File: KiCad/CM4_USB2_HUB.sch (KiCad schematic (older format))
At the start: 33 parts, among them IC1 USB2517-JZX, J10 72309-8014BLF, J11 10104110-0001LF, J12 SS-52100-002, J8 Conn_02x05_Odd_Even, J9 Conn_02x05_Odd_Even, U3 FSUSB42MUX, Y1 24MHz

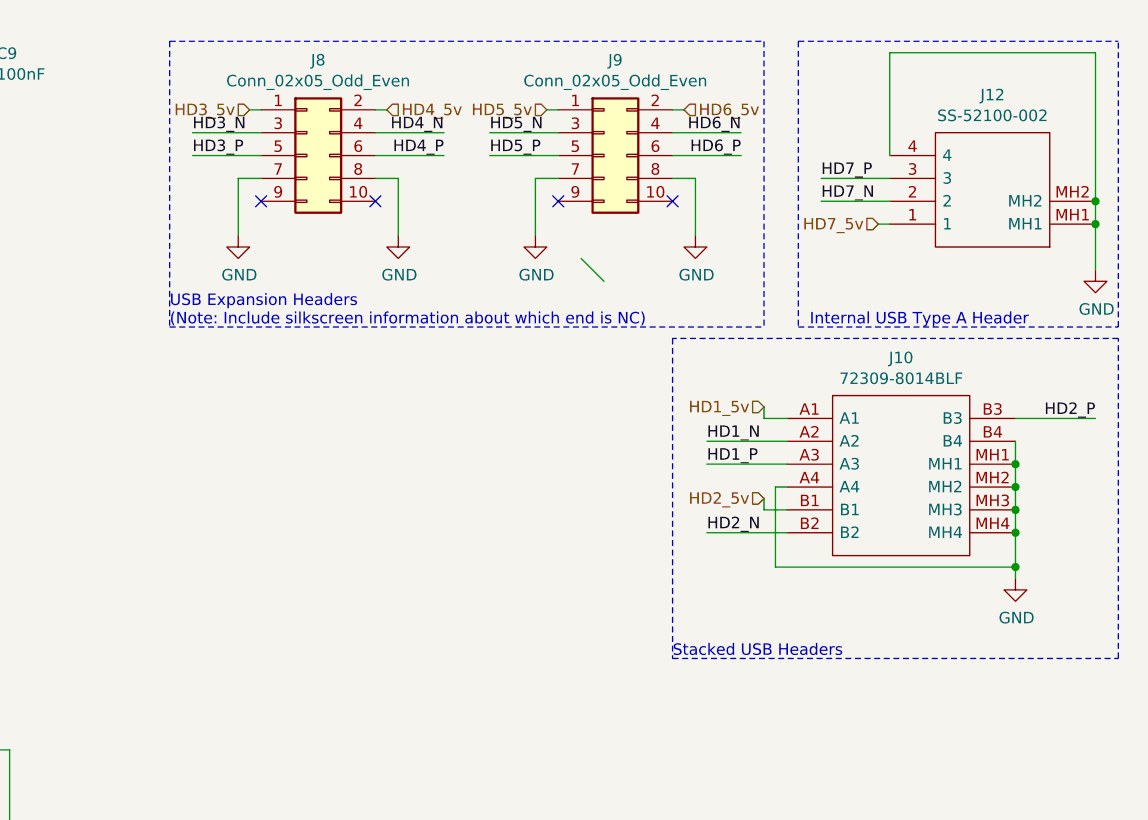
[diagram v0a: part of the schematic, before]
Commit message: Added second USB dual-stack header and fixed some library references.
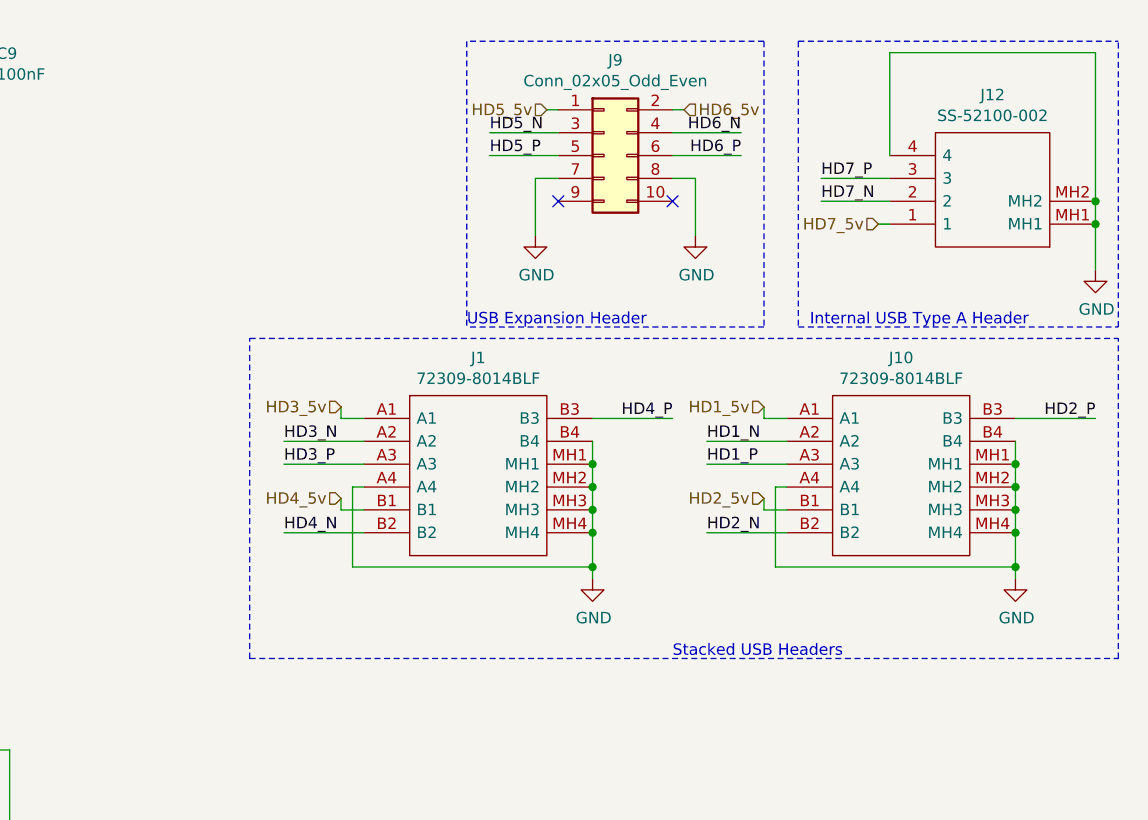
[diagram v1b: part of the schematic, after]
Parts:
- removed J8: Conn_02x05_Odd_Even, CM4_MATX:PinHeader_2x05_P2.54mm_Vertical, symbol Connector_Generic:Conn_02x05_Odd_Even
- added J1: 72309-8014BLF, CM4_MATX:723098014BLF, symbol CM4_MATX:72309-8014BLF
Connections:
- net GND: now also J1.A4, J1.B4, J1.MH1, J1.MH2, J1.MH3, J1.MH4
- net HD3_5v: now also J1.A1
- net HD3_N: now also J1.A2
- net HD3_P: now also J1.A3
- net HD4_5v: now also J1.B1
- net HD4_N: now also J1.B2
- net HD4_P: now also J1.B3
- no-connect marks 19 -> 17
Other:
- note added: "USB Expansion Header"
- note removed: "USB Expansion Headers\n(Note: Include silkscreen information about which end is NC)"
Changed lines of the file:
@@
 	9350 2750 9700 2750
 Wire Notes Line
-	9200 3300 11150 3300
-Wire Notes Line
 	11150 3300 11150 1900
-Wire Notes Line
-	11150 1900 9200 1900
-Wire Notes Line
-	9200 1900 9200 3300
 Text Notes 9200 3300 0    50   ~ 0
 Stacked USB Headers
@@
 	1    0    0    -1
 $EndComp
-$Comp
-L power:GND #PWR0126
-U 1 1 5FF0B6D3
-P 8000 1450
-F 0 "#PWR0126" H 8000 1200 50  0001 C CNN
-F 1 "GND" H 8005 1277 50  0000 C CNN
-F 2 "" H 8000 1450 50  0001 C CNN
-F 3 "" H 8000 1450 50  0001 C CNN
-	1    8000 1450
-	1    0    0    -1
-$EndComp
-$Comp
-L power:GND #PWR0127
-U 1 1 5FF0AFE9
-P 7300 1450
-F 0 "#PWR0127" H 7300 1200 50  0001 C CNN
-F 1 "GND" H 7305 1277 50  0000 C CNN
-F 2 "" H 7300 1450 50  0001 C CNN
-F 3 "" H 7300 1450 50  0001 C CNN
-	1    7300 1450
-	1    0    0    -1
-$EndComp
-NoConn ~ 7400 1300
-NoConn ~ 7900 1300
-Wire Wire Line
-	8000 1200 8000 1450
-Wire Wire Line
-	7900 1200 8000 1200
-Wire Wire Line
-	7300 1200 7300 1450
-Wire Wire Line
-	7400 1200 7300 1200
-Wire Wire Line
-	7400 1100 7100 1100
-Wire Wire Line
-	7100 1000 7400 1000
-Wire Wire Line
-	7900 1000 8200 1000
-Wire Wire Line
-	8200 1100 7900 1100
 Wire Wire Line
 	8700 1100 8400 1100
@@
 Text Label 8400 1000 0    50   ~ 0
 HD5_N
-Text Label 8200 1100 2    50   ~ 0
-HD4_P
-Text Label 8200 1000 2    50   ~ 0
-HD4_N
-Text Label 7100 1100 0    50   ~ 0
-HD3_P
-Text Label 7100 1000 0    50   ~ 0
-HD3_N
-$Comp
-L Connector_Generic:Conn_02x05_Odd_Even J8
-U 1 1 5FEAE38F
-P 7600 1100
-F 0 "J8" H 7650 1517 50  0000 C CNN
-F 1 "Conn_02x05_Odd_Even" H 7650 1426 50  0000 C CNN
-F 2 "CM4_MATX:PinHeader_2x05_P2.54mm_Vertical" H 7600 1100 50  0001 C CNN
-F 3 "~" H 7600 1100 50  0001 C CNN
-	1    7600 1100
-	1    0    0    -1
-$EndComp
 Wire Notes Line
 	9600 600  9600 1850
-Text Notes 7000 1850 0    50   ~ 0
-USB Expansion Headers\n(Note: Include silkscreen information about which end is NC)
+Text Notes 8300 1850 0    50   ~ 0
+USB Expansion Header
 Wire Wire Line
 	4850 3900 5200 3900
@@
 Wire Notes Line
 	9750 1850 11150 1850
-Text HLabel 7350 900  0    50   Input ~ 0
-HD3_5v
-Wire Wire Line
-	7350 900  7400 900
-Text HLabel 7950 900  2    50   Input ~ 0
-HD4_5v
 Text HLabel 8650 900  0    50   Input ~ 0
 HD5_5v
 Wire Wire Line
 	8650 900  8700 900
-Wire Wire Line
-	7900 900  7950 900
 Text HLabel 9250 900  2    50   Input ~ 0
 HD6_5v
 Wire Wire Line
 	9250 900  9200 900
-Wire Notes Line
-	7000 600  7000 1850
-Wire Notes Line
-	7000 600  9600 600
-Wire Notes Line
-	7000 1850 9600 1850
 Text HLabel 9600 2600 0    50   Input ~ 0
 HD2_5v
@@
 Text Notes 7550 6500 0    50   ~ 0
 USB OTG/Slave connector for eMMC flashing on support CM4s
-Entry Wire Line
-	8800 1550 8900 1650
+$Comp
+L CM4_MATX:72309-8014BLF J1
+U 1 1 626F6425
+P 7850 2250
+F 0 "J1" H 8350 2515 50  0000 C CNN
+F 1 "72309-8014BLF" H 8350 2424 50  0000 C CNN
+F 2 "CM4_MATX:723098014BLF" H 8700 2350 50  0001 L CNN
+F 3 "https://cdn.amphenol-icc.com/media/wysiwyg/files/drawing/72309.pdf" H 8700 2250 50  0001 L CNN
+F 4 "USB Connectors 8P R/A RECPT" H 8700 2150 50  0001 L CNN "Description"
+F 5 "15" H 8700 2050 50  0001 L CNN "Height"
+F 6 "649-72309-8014BLF" H 8700 1950 50  0001 L CNN "Mouser Part Number"
+F 7 "https://www.mouser.co.uk/ProductDetail/Amphenol-FCI/72309-8014BLF?qs=D%252By4jQJzx8Iuk4xBbyHrOA%3D%3D" H 8700 1850 50  0001 L CNN "Mouser Price/Stock"
+F 8 "Amphenol" H 8700 1750 50  0001 L CNN "Manufacturer_Name"
+F 9 "72309-8014BLF" H 8700 1650 50  0001 L CNN "Manufacturer_Part_Number"
+	1    7850 2250
+	1    0    0    -1
+$EndComp
+Wire Wire Line
+	8850 2450 8850 2550
+Connection ~ 8850 2550
+Wire Wire Line
+	8850 2550 8850 2650
+Connection ~ 8850 2650
+Wire Wire Line
+	8850 2650 8850 2750
+Connection ~ 8850 2750
+Wire Wire Line
+	8850 2750 8850 2900
+$Comp
+L power:GND #PWR0103
+U 1 1 626F6432
+P 8850 2950
+F 0 "#PWR0103" H 8850 2700 50  0001 C CNN
+F 1 "GND" H 8855 2777 50  0000 C CNN
+F 2 "" H 8850 2950 50  0001 C CNN
+F 3 "" H 8850 2950 50  0001 C CNN
+	1    8850 2950
+	1    0    0    -1
+$EndComp
+Text Label 7500 2350 0    50   ~ 0
+HD3_N
+Text Label 7500 2450 0    50   ~ 0
+HD3_P
+Text Label 7500 2750 0    50   ~ 0
+HD4_N
+Text Label 9200 2250 2    50   ~ 0
+HD4_P
+Wire Wire Line
+	9200 2250 8850 2250
+Wire Wire Line
+	7500 2350 7850 2350
+Wire Wire Line
+	7850 2450 7500 2450
+Wire Wire Line
+	7850 2550 7800 2550
+Wire Wire Line
+	7800 2550 7800 2900
+Wire Wire Line
+	7800 2900 8850 2900
+Connection ~ 8850 2900
+Wire Wire Line
+	8850 2900 8850 2950
+Wire Wire Line
+	8850 2350 8850 2450
+Connection ~ 8850 2450
+Wire Wire Line
+	7500 2750 7850 2750
+Text HLabel 7750 2200 0    50   Input ~ 0
+HD3_5v
+Text HLabel 7750 2600 0    50   Input ~ 0
+HD4_5v
+Wire Wire Line
+	7750 2600 7750 2650
+Wire Wire Line
+	7750 2650 7850 2650
+Wire Wire Line
+	7750 2200 7750 2250
+Wire Wire Line
+	7750 2250 7850 2250
+Wire Notes Line
+	7350 3300 7350 1900
+Wire Notes Line
+	7350 3300 11150 3300
+Wire Notes Line
+	7350 1900 11150 1900
+Wire Notes Line
+	8300 600  8300 1850
+Wire Notes Line
+	9600 600  8300 600
+Wire Notes Line
+	9600 1850 8300 1850
 $EndSCHEMATC

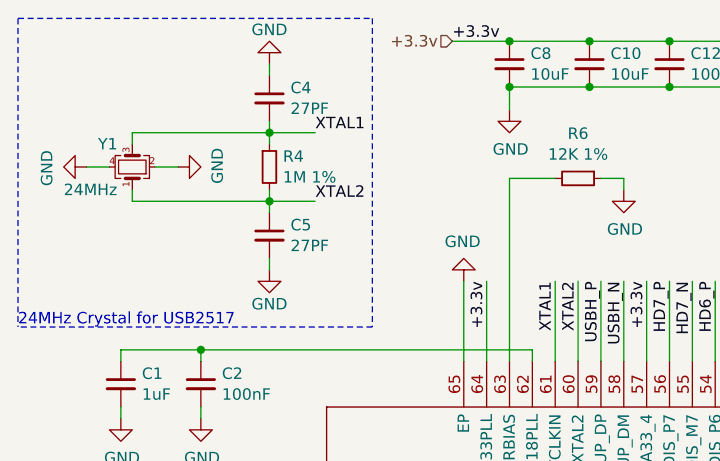
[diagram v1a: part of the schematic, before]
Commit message: PCIe Wiring, resistor value adjustments, and a bunch of small ERC fixes.
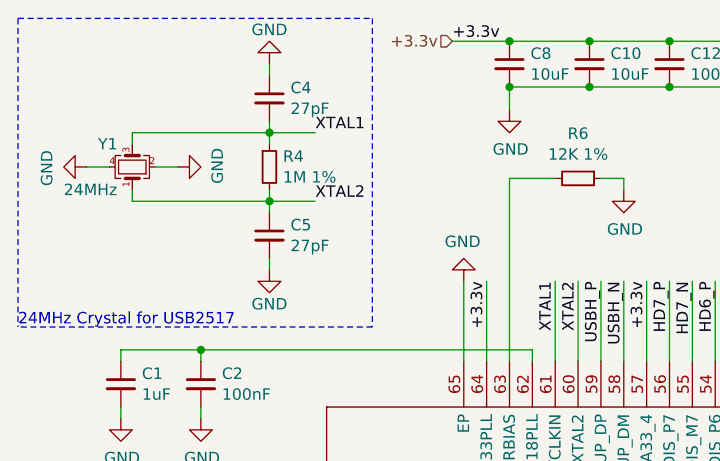
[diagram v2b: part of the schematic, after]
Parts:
- C4, C5: value 27PF -> 27pF
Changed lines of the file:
@@
 P 1600 1450
 F 0 "C5" H 1692 1496 50  0000 L CNN
-F 1 "27PF" H 1692 1405 50  0000 L CNN
+F 1 "27pF" H 1692 1405 50  0000 L CNN
 F 2 "" H 1600 1450 50  0001 C CNN
 F 3 "~" H 1600 1450 50  0001 C CNN
@@
 P 1600 850
 F 0 "C4" H 1692 896 50  0000 L CNN
-F 1 "27PF" H 1692 805 50  0000 L CNN
+F 1 "27pF" H 1692 805 50  0000 L CNN
 F 2 "" H 1600 850 50  0001 C CNN
 F 3 "~" H 1600 850 50  0001 C CNN

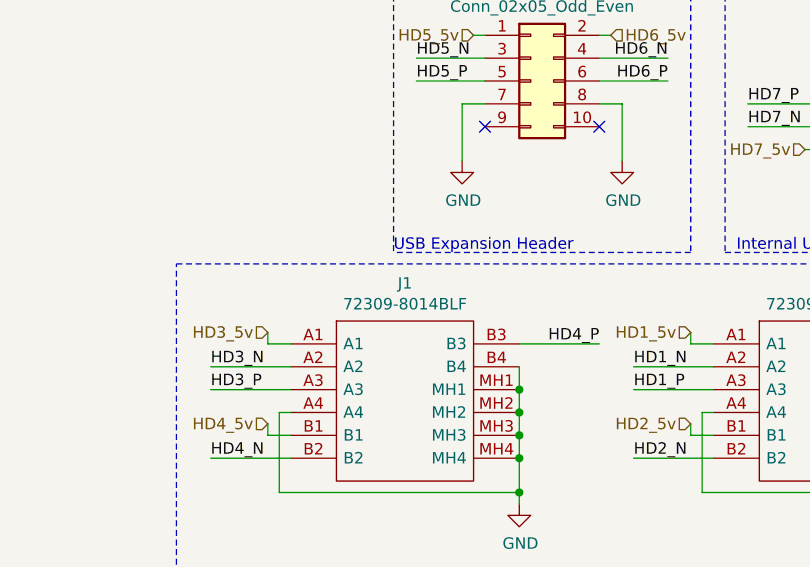
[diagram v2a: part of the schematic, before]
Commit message: Updated CM4 footprints/symbols, mounting holes
This is in a bid to make it more manufactuerable by reducing the need for explanations and questions.
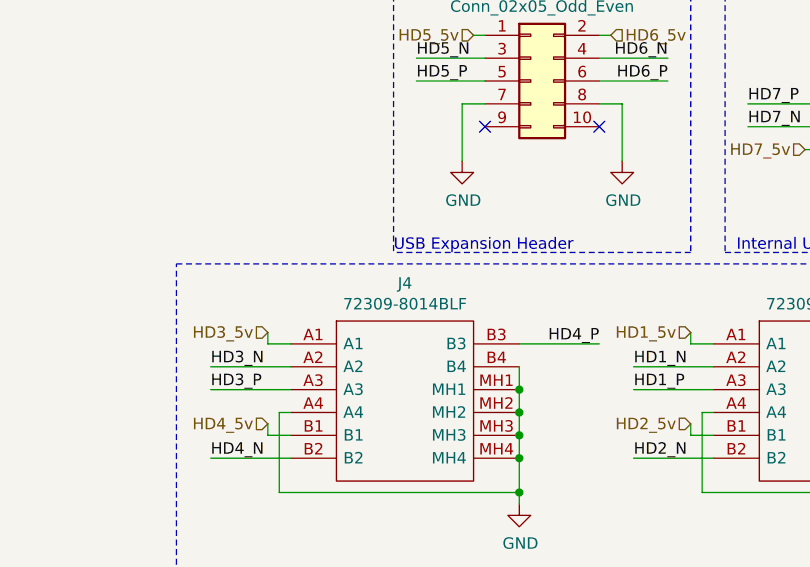
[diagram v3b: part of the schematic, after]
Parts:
- renumbered J1 to J4
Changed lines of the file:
@@
 Sheet 8 16
 Title "CM4_MATX: USB Hub and Ports"
-Date "2020-12-28"
+Date "2021-02-08"
 Rev "0.1"
 Comp "Copyright Oliver Møller/@TheGuyDanish 2020, CERN OHL-P v2"
@@
 Text Notes 7550 6500 0    50   ~ 0
 USB OTG/Slave connector for eMMC flashing on support CM4s
-$Comp
-L CM4_MATX:72309-8014BLF J1
+Wire Wire Line
+	8850 2450 8850 2550
+Connection ~ 8850 2550
+Wire Wire Line
+	8850 2550 8850 2650
+Connection ~ 8850 2650
+Wire Wire Line
+	8850 2650 8850 2750
+Connection ~ 8850 2750
+Wire Wire Line
+	8850 2750 8850 2900
+$Comp
+L power:GND #PWR0103
+U 1 1 626F6432
+P 8850 2950
+F 0 "#PWR0103" H 8850 2700 50  0001 C CNN
+F 1 "GND" H 8855 2777 50  0000 C CNN
+F 2 "" H 8850 2950 50  0001 C CNN
+F 3 "" H 8850 2950 50  0001 C CNN
+	1    8850 2950
+	1    0    0    -1
+$EndComp
+Text Label 7500 2350 0    50   ~ 0
+HD3_N
+Text Label 7500 2450 0    50   ~ 0
+HD3_P
+Text Label 7500 2750 0    50   ~ 0
+HD4_N
+Text Label 9200 2250 2    50   ~ 0
+HD4_P
+Wire Wire Line
+	9200 2250 8850 2250
+Wire Wire Line
+	7500 2350 7850 2350
+Wire Wire Line
+	7850 2450 7500 2450
+Wire Wire Line
+	7850 2550 7800 2550
+Wire Wire Line
+	7800 2550 7800 2900
+Wire Wire Line
+	7800 2900 8850 2900
+Connection ~ 8850 2900
+Wire Wire Line
+	8850 2900 8850 2950
+Wire Wire Line
+	8850 2350 8850 2450
+Connection ~ 8850 2450
+Wire Wire Line
+	7500 2750 7850 2750
+Text HLabel 7750 2200 0    50   Input ~ 0
+HD3_5v
+Text HLabel 7750 2600 0    50   Input ~ 0
+HD4_5v
+Wire Wire Line
+	7750 2600 7750 2650
+Wire Wire Line
+	7750 2650 7850 2650
+Wire Wire Line
+	7750 2200 7750 2250
+Wire Wire Line
+	7750 2250 7850 2250
+Wire Notes Line
+	7350 3300 7350 1900
+Wire Notes Line
+	7350 3300 11150 3300
+Wire Notes Line
+	7350 1900 11150 1900
+Wire Notes Line
+	8300 600  8300 1850
+Wire Notes Line
+	9600 600  8300 600
+Wire Notes Line
+	9600 1850 8300 1850
+$Comp
+L CM4_MATX:72309-8014BLF J4
 U 1 1 626F6425
 P 7850 2250
-F 0 "J1" H 8350 2515 50  0000 C CNN
+F 0 "J4" H 8350 2515 50  0000 C CNN
 F 1 "72309-8014BLF" H 8350 2424 50  0000 C CNN
 F 2 "CM4_MATX:723098014BLF" H 8700 2350 50  0001 L CNN
@@
 	1    0    0    -1
 $EndComp
-Wire Wire Line
-	8850 2450 8850 2550
-Connection ~ 8850 2550
-Wire Wire Line
-	8850 2550 8850 2650
-Connection ~ 8850 2650
-Wire Wire Line
-	8850 2650 8850 2750
-Connection ~ 8850 2750
-Wire Wire Line
-	8850 2750 8850 2900
-$Comp
-L power:GND #PWR0103
-U 1 1 626F6432
-P 8850 2950
-F 0 "#PWR0103" H 8850 2700 50  0001 C CNN
-F 1 "GND" H 8855 2777 50  0000 C CNN
-F 2 "" H 8850 2950 50  0001 C CNN
-F 3 "" H 8850 2950 50  0001 C CNN
-	1    8850 2950
-	1    0    0    -1
-$EndComp
-Text Label 7500 2350 0    50   ~ 0
-HD3_N
-Text Label 7500 2450 0    50   ~ 0
-HD3_P
-Text Label 7500 2750 0    50   ~ 0
-HD4_N
-Text Label 9200 2250 2    50   ~ 0
-HD4_P
-Wire Wire Line
-	9200 2250 8850 2250
-Wire Wire Line
-	7500 2350 7850 2350
-Wire Wire Line
-	7850 2450 7500 2450
-Wire Wire Line
-	7850 2550 7800 2550
-Wire Wire Line
-	7800 2550 7800 2900
-Wire Wire Line
-	7800 2900 8850 2900
-Connection ~ 8850 2900
-Wire Wire Line
-	8850 2900 8850 2950
-Wire Wire Line
-	8850 2350 8850 2450
-Connection ~ 8850 2450
-Wire Wire Line
-	7500 2750 7850 2750
-Text HLabel 7750 2200 0    50   Input ~ 0
-HD3_5v
-Text HLabel 7750 2600 0    50   Input ~ 0
-HD4_5v
-Wire Wire Line
-	7750 2600 7750 2650
-Wire Wire Line
-	7750 2650 7850 2650
-Wire Wire Line
-	7750 2200 7750 2250
-Wire Wire Line
-	7750 2250 7850 2250
-Wire Notes Line
-	7350 3300 7350 1900
-Wire Notes Line
-	7350 3300 11150 3300
-Wire Notes Line
-	7350 1900 11150 1900
-Wire Notes Line
-	8300 600  8300 1850
-Wire Notes Line
-	9600 600  8300 600
-Wire Notes Line
-	9600 1850 8300 1850
 $EndSCHEMATC

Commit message: Started picking passive components, overhauled library
Cleaned up a bunch of schematic library references.
Added datasheets, descriptions for a lot of existing parts.
Picked most capacitor parts, still a couple left.
Cleaned up a fair few footprint references.
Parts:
- removed C1, C3: 1uF, symbol Device:C_Small
- C10, C8: footprint (none) -> CM4_MATX:C_0603_1608Metric_Pad1.08x0.95mm_HandSolder; symbol Device:C_Small -> CM4_MATX:C_Small; Description (none) -> 6.3V 10uF X5R 0603 20% Tol; Mfr. (none) -> Samsung; Mfr. No (none) -> CL10A106MQ8NNNC; Mouser Part Number (none) -> 187-CL10A106MQ8NNNC; Mouser Price/Stock (none) -> https://www.mouser.co.uk/ProductDetail/Samsung-Electro-Mech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
- C12, C14, C16, C19, C2, C21, C23, C6, C7, C9: footprint (none) -> CM4_MATX:C_0402_1005Metric_Pad0.74x0.62mm_HandSolder; symbol Device:C_Small -> CM4_MATX:C_Small; Description (none) -> 10V 0.1uF X5R 0402 20% Tol; Mfr. (none) -> AVX; Mfr. No (none) -> 0402ZD104MAT4A; Mouser Part Number (none) -> 581-0402ZD104MAT4A; Mouser Price/Stock (none) -> https://www.mouser.co.uk/ProductDetail/AVX/0402ZD104MAT4A/?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
- C4, C5: symbol Device:C_Small -> CM4_MATX:C_Small; Description (none) -> Load Capacitors for Y1 Crystal
- IC1: Height 1 -> (none); Manufacturer_Name Microchip -> (none); Manufacturer_Part_Number USB2517-JZX -> (none); Mfr. (none) -> Microchip; Mfr. No (none) -> USB2517-JZX
- J10, J4: Height 15 -> (none); Manufacturer_Name Amphenol -> (none); Manufacturer_Part_Number 72309-8014BLF -> (none); Mfr. (none) -> Amphenol; Mfr. No (none) -> 72309-8014BLF
- J11: Height 2.98 -> (none); Manufacturer_Name Amphenol -> (none); Manufacturer_Part_Number 10104110-0001LF -> (none); Mfr. (none) -> Amphenol; Mfr. No (none) -> 10104110-0001LF
- J12: Height 15.4 -> (none); Manufacturer_Name Stewart Connector -> (none); Manufacturer_Part_Number SS-52100-002 -> (none); Mfr. (none) -> Stewart Connector; Mfr. No (none) -> SS-52100-002
- J9: symbol Connector_Generic:Conn_02x05_Odd_Even -> CM4_MATX:Conn_02x05_Odd_Even; Description (none) -> Standard 2.54mm (100mil)-separated pins
- R10, R11, R12, R3, R4, R6, R8, R9: symbol Device:R_Small -> CM4_MATX:R_Small
- R13: footprint (none) -> CM4_MATX:R_0603_1608Metric_Pad0.98x0.95mm_HandSolder; symbol Device:R_Small -> CM4_MATX:R_Small
- U3: Height 1.1 -> (none); Manufacturer_Name ON Semiconductor -> (none); Manufacturer_Part_Number FSUSB42MUX -> (none); Mfr. (none) -> ON Semiconductor; Mfr. No (none) -> FSUSB42MUX
- Y1: footprint (none) -> CM4_MATX:Crystal_SMD_3225-4Pin_3.2x2.5mm_HandSoldering; symbol Device:Crystal_GND24_Small -> CM4_MATX:Crystal_GND24_Small; Description (none) -> Crystals 24MHZ 9pF +/-10ppm +/-20ppm -40 C 105C; Mfr. (none) -> ECS; Mfr. No (none) -> ECS-240-9-33B-CTP-TR; Mouser Part Number (none) -> 520-ECS240933BCTP-TR; Mouser Price/Stock (none) -> https://www.mouser.co.uk/ProductDetail/ECS/ECS-240-9-33B-CT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
